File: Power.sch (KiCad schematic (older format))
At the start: 11 parts, among them P1 24-pin Mini-Fit Jr., SW1 SWITCH_INV

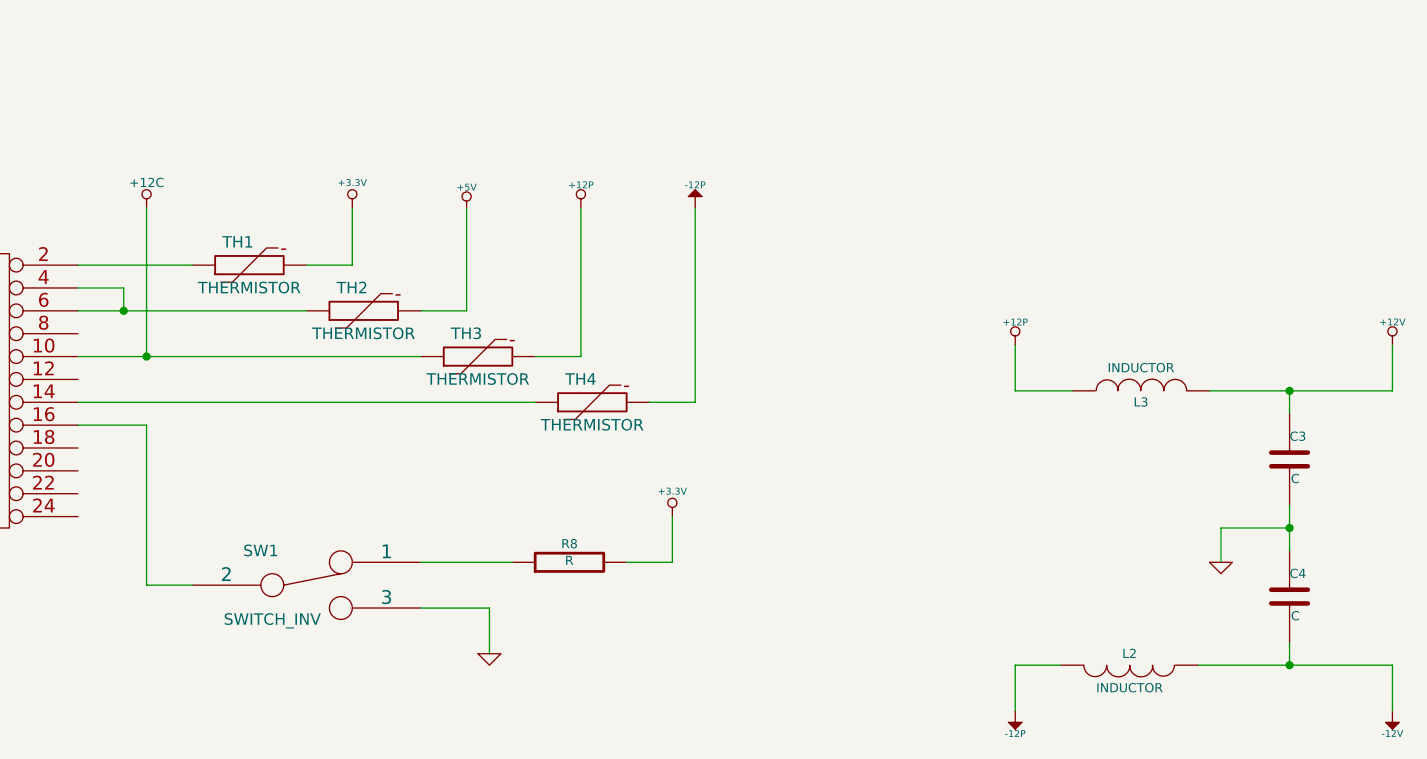
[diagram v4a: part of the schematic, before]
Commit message: Associated and placed the Power Filter Module
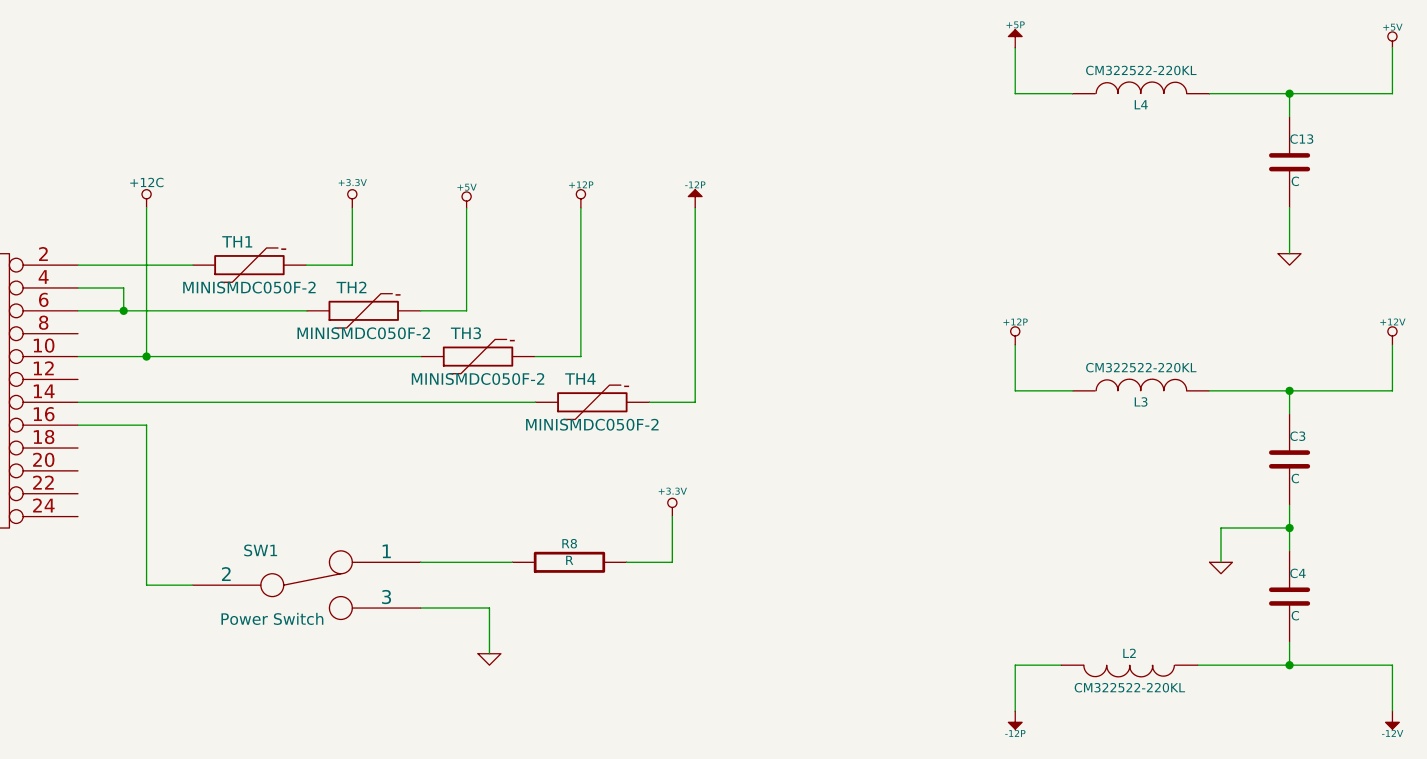
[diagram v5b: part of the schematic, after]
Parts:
- added C13: C, symbol C
- added L4: CM322522-220KL, symbol INDUCTOR
- L2, L3: value INDUCTOR -> CM322522-220KL; MFG Name (none) -> Bourns
- SW1: value SWITCH_INV -> Power Switch; MFG Name (none) -> C&K Components; MFG Part Number (none) -> OS102011MA1QN1
- TH1, TH2, TH3, TH4: value THERMISTOR -> MINISMDC050F-2; MFG Name (none) -> TE Connectivity; MFG Part Number (none) -> MINISMDC050F-2
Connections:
- net +5V: now also C13.1, L4.2
- net GND: now also C13.2
- new net +5P: L4.1
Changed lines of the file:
@@
 P 3500 3200
 F 0 "SW1" H 3300 3350 50  0000 C CNN
-F 1 "SWITCH_INV" H 3350 3050 50  0000 C CNN
+F 1 "Power Switch" H 3350 3050 50  0000 C CNN
 F 2 "" H 3500 3200 60  0000 C CNN
 F 3 "" H 3500 3200 60  0000 C CNN
+F 4 "C&K Components" H 3500 3200 60  0001 C CNN "MFG Name"
+F 5 "OS102011MA1QN1" H 3500 3200 60  0001 C CNN "MFG Part Number"
 	1    3500 3200
 	1    0    0    -1
@@
 $EndComp
 $Comp
-L +12P #PWR15
+L +12P #PWR16
 U 1 1 52F29CEF
 P 6600 2150
-F 0 "#PWR15" H 6600 2120 30  0001 C CNN
+F 0 "#PWR16" H 6600 2120 30  0001 C CNN
 F 1 "+12P" H 6600 2250 30  0000 C CNN
 F 2 "" H 6600 2150 60  0000 C CNN
@@
 $EndComp
 $Comp
-L -12P #PWR16
+L -12P #PWR17
 U 1 1 52F29CF5
 P 6600 3750
-F 0 "#PWR16" H 6600 3880 20  0001 C CNN
+F 0 "#PWR17" H 6600 3880 20  0001 C CNN
 F 1 "-12P" H 6600 3850 30  0000 C CNN
 F 2 "" H 6600 3750 60  0000 C CNN
@@
 $EndComp
 $Comp
-L GND #PWR17
+L GND #PWR18
 U 1 1 52F29CFB
 P 7500 3100
-F 0 "#PWR17" H 7500 3100 30  0001 C CNN
+F 0 "#PWR18" H 7500 3100 30  0001 C CNN
 F 1 "GND" H 7500 3030 30  0001 C CNN
 F 2 "" H 7500 3100 60  0000 C CNN
@@
 P 7150 2350
 F 0 "L3" V 7100 2350 40  0000 C CNN
-F 1 "INDUCTOR" V 7250 2350 40  0000 C CNN
+F 1 "CM322522-220KL" V 7250 2350 40  0000 C CNN
 F 2 "" H 7150 2350 60  0000 C CNN
 F 3 "" H 7150 2350 60  0000 C CNN
+F 4 "Bourns" H 7150 2350 60  0001 C CNN "MFG Name"
 	1    7150 2350
 	0    -1   -1   0
-$EndComp
-$Comp
-L INDUCTOR L2
-U 1 1 52F29D07
-P 7100 3550
-F 0 "L2" V 7050 3550 40  0000 C CNN
-F 1 "INDUCTOR" V 7200 3550 40  0000 C CNN
-F 2 "" H 7100 3550 60  0000 C CNN
-F 3 "" H 7100 3550 60  0000 C CNN
-	1    7100 3550
-	0    1    1    0
 $EndComp
 $Comp
@@
 Connection ~ 7800 3550
 $Comp
-L +12V #PWR18
+L +12V #PWR21
 U 1 1 52F29D29
 P 8250 2150
-F 0 "#PWR18" H 8250 2100 20  0001 C CNN
+F 0 "#PWR21" H 8250 2100 20  0001 C CNN
 F 1 "+12V" H 8250 2250 30  0000 C CNN
 F 2 "" H 8250 2150 60  0000 C CNN
@@
 $EndComp
 $Comp
-L -12V #PWR19
+L -12V #PWR22
 U 1 1 52F29D2F
 P 8250 3750
-F 0 "#PWR19" H 8250 3880 20  0001 C CNN
+F 0 "#PWR22" H 8250 3880 20  0001 C CNN
 F 1 "-12V" H 8250 3850 30  0000 C CNN
 F 2 "" H 8250 3750 60  0000 C CNN
@@
 P 3250 1800
 F 0 "TH1" V 3350 1850 50  0000 C CNN
-F 1 "THERMISTOR" V 3150 1800 50  0000 C CNN
+F 1 "MINISMDC050F-2" V 3150 1800 50  0000 C CNN
 F 2 "" H 3250 1800 60  0000 C CNN
 F 3 "" H 3250 1800 60  0000 C CNN
+F 4 "TE Connectivity" H 3250 1800 60  0001 C CNN "MFG Name"
+F 5 "MINISMDC050F-2" H 3250 1800 60  0001 C CNN "MFG Part Number"
 	1    3250 1800
 	0    -1   -1   0
@@
 $Comp
 L THERMISTOR TH2
-U 1 1 52FBEC68
+U 1 1 530A209B
 P 3750 2000
 F 0 "TH2" V 3850 2050 50  0000 C CNN
-F 1 "THERMISTOR" V 3650 2000 50  0000 C CNN
+F 1 "MINISMDC050F-2" V 3650 2000 50  0000 C CNN
 F 2 "" H 3750 2000 60  0000 C CNN
 F 3 "" H 3750 2000 60  0000 C CNN
+F 4 "TE Connectivity" H 3750 2000 60  0001 C CNN "MFG Name"
+F 5 "MINISMDC050F-2" H 3750 2000 60  0001 C CNN "MFG Part Number"
 	1    3750 2000
 	0    -1   -1   0
@@
 $Comp
 L THERMISTOR TH3
-U 1 1 52FBEC73
+U 1 1 530A20B9
 P 4250 2200
 F 0 "TH3" V 4350 2250 50  0000 C CNN
-F 1 "THERMISTOR" V 4150 2200 50  0000 C CNN
+F 1 "MINISMDC050F-2" V 4150 2200 50  0000 C CNN
 F 2 "" H 4250 2200 60  0000 C CNN
 F 3 "" H 4250 2200 60  0000 C CNN
+F 4 "TE Connectivity" H 4250 2200 60  0001 C CNN "MFG Name"
+F 5 "MINISMDC050F-2" H 4250 2200 60  0001 C CNN "MFG Part Number"
 	1    4250 2200
 	0    -1   -1   0
@@
 $Comp
 L THERMISTOR TH4
-U 1 1 52FBEC7E
+U 1 1 530A20C8
 P 4750 2400
 F 0 "TH4" V 4850 2450 50  0000 C CNN
-F 1 "THERMISTOR" V 4650 2400 50  0000 C CNN
+F 1 "MINISMDC050F-2" V 4650 2400 50  0000 C CNN
 F 2 "" H 4750 2400 60  0000 C CNN
 F 3 "" H 4750 2400 60  0000 C CNN
+F 4 "TE Connectivity" H 4750 2400 60  0001 C CNN "MFG Name"
+F 5 "MINISMDC050F-2" H 4750 2400 60  0001 C CNN "MFG Part Number"
 	1    4750 2400
 	0    -1   -1   0
 $EndComp
+$Comp
+L INDUCTOR L4
+U 1 1 530A2152
+P 7150 1050
+F 0 "L4" V 7100 1050 40  0000 C CNN
+F 1 "CM322522-220KL" V 7250 1050 40  0000 C CNN
+F 2 "" H 7150 1050 60  0000 C CNN
+F 3 "" H 7150 1050 60  0000 C CNN
+F 4 "Bourns" H 7150 1050 60  0001 C CNN "MFG Name"
+	1    7150 1050
+	0    -1   -1   0
+$EndComp
+$Comp
+L C C13
+U 1 1 530A2158
+P 7800 1350
+F 0 "C13" H 7800 1450 40  0000 L CNN
+F 1 "C" H 7806 1265 40  0000 L CNN
+F 2 "" H 7838 1200 30  0000 C CNN
+F 3 "" H 7800 1350 60  0000 C CNN
+	1    7800 1350
+	1    0    0    -1
+$EndComp
+Wire Wire Line
+	7450 1050 8250 1050
+Wire Wire Line
+	7800 1050 7800 1150
+Wire Wire Line
+	7800 1550 7800 1750
+Wire Wire Line
+	6850 1050 6600 1050
+Wire Wire Line
+	6600 1050 6600 850
+Wire Wire Line
+	8250 1050 8250 850
+Connection ~ 7800 1050
+$Comp
+L +5P #PWR15
+U 1 1 530A216D
+P 6600 850
+F 0 "#PWR15" H 6600 980 20  0001 C CNN
+F 1 "+5P" H 6600 950 30  0000 C CNN
+F 2 "" H 6600 850 60  0000 C CNN
+F 3 "" H 6600 850 60  0000 C CNN
+	1    6600 850
+	1    0    0    -1
+$EndComp
+$Comp
+L +5V #PWR20
+U 1 1 530A2195
+P 8250 850
+F 0 "#PWR20" H 8250 940 20  0001 C CNN
+F 1 "+5V" H 8250 940 30  0000 C CNN
+F 2 "" H 8250 850 60  0000 C CNN
+F 3 "" H 8250 850 60  0000 C CNN
+	1    8250 850
+	1    0    0    -1
+$EndComp
+$Comp
+L GND #PWR19
+U 1 1 530A21B1
+P 7800 1750
+F 0 "#PWR19" H 7800 1750 30  0001 C CNN
+F 1 "GND" H 7800 1680 30  0001 C CNN
+F 2 "" H 7800 1750 60  0000 C CNN
+F 3 "" H 7800 1750 60  0000 C CNN
+	1    7800 1750
+	1    0    0    -1
+$EndComp
+$Comp
+L INDUCTOR L2
+U 1 1 530A21BD
+P 7100 3550
+F 0 "L2" V 7050 3550 40  0000 C CNN
+F 1 "CM322522-220KL" V 7200 3550 40  0000 C CNN
+F 2 "" H 7100 3550 60  0000 C CNN
+F 3 "" H 7100 3550 60  0000 C CNN
+F 4 "Bourns" H 7100 3550 60  0001 C CNN "MFG Name"
+	1    7100 3550
+	0    1    1    0
+$EndComp
 $EndSCHEMATC

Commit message: Updates from Layout Work Session 5 video
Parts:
- added TP1: CONN_1, symbol CONN_1
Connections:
- net GND: now also TP1.1
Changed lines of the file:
@@
 $EndComp
 Wire Wire Line
-	1700 1900 900  1900
+	900  1900 1700 1900
 Wire Wire Line
 	1700 2000 1500 2000
@@
 	0    1    1    0
 $EndComp
+$Comp
+L CONN_1 TP1
+U 1 1 53163E2C
+P 5500 4150
+F 0 "TP1" H 5580 4150 40  0000 L CNN
+F 1 "CONN_1" H 5500 4205 30  0001 C CNN
+F 2 "" H 5500 4150 60  0000 C CNN
+F 3 "" H 5500 4150 60  0000 C CNN
+	1    5500 4150
+	-1   0    0    1
+$EndComp
+$Comp
+L GND #PWR021
+U 1 1 53163E4D
+P 5750 4350
+F 0 "#PWR021" H 5750 4350 30  0001 C CNN
+F 1 "GND" H 5750 4280 30  0001 C CNN
+F 2 "" H 5750 4350 60  0000 C CNN
+F 3 "" H 5750 4350 60  0000 C CNN
+	1    5750 4350
+	1    0    0    -1
+$EndComp
+Wire Wire Line
+	5650 4150 5750 4150
+Wire Wire Line
+	5750 4150 5750 4350
 $EndSCHEMATC

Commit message: Updates from Layout Work Session 6 video
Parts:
- added JP1, JP2, JP3, JP4: JUMPER, symbol JUMPER
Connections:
- net +5P: now also TH2.2
- net +5V: no longer TH2.2
- net GND: now also JP1.1, JP2.1, JP3.1, JP4.1
- net at P1.12 (P12): now also P1.2 (P2), TH1.1
- new net AGND: JP1.2
- new net GND_LED: JP3.2
- new net GND_PWR: JP2.2
- new net GND_RELAY: JP4.2
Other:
- note added: "Star Point"
- moved on the sheet: TP1
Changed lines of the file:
@@
-	1    0    0    -1
-$EndComp
-$Comp
-L +3.3V #PWR07
-U 1 1 52F29C8B
-P 3700 1550
-F 0 "#PWR07" H 3700 1510 30  0001 C CNN
-F 1 "+3.3V" H 3700 1660 30  0000 C CNN
-F 2 "" H 3700 1550 60  0000 C CNN
-F 3 "" H 3700 1550 60  0000 C CNN
-	1    3700 1550
-	1    0    0    -1
-$EndComp
-$Comp
-L +5V #PWR08
-U 1 1 52F29C91
-P 4200 1550
-F 0 "#PWR08" H 4200 1640 20  0001 C CNN
-F 1 "+5V" H 4200 1640 30  0000 C CNN
-F 2 "" H 4200 1550 60  0000 C CNN
-F 3 "" H 4200 1550 60  0000 C CNN
-	1    4200 1550
 	1    0    0    -1
 $EndComp
@@
 	4700 2200 4700 1550
 $Comp
-L +12P #PWR09
+L +12P #PWR07
 U 1 1 52F29CC3
 P 4700 1550
-F 0 "#PWR09" H 4700 1520 30  0001 C CNN
+F 0 "#PWR07" H 4700 1520 30  0001 C CNN
 F 1 "+12P" H 4700 1650 30  0000 C CNN
 F 2 "" H 4700 1550 60  0000 C CNN
@@
 	5200 2400 5200 1550
 $Comp
-L -12P #PWR010
+L -12P #PWR08
 U 1 1 52F29CCB
 P 5200 1550
-F 0 "#PWR010" H 5200 1680 20  0001 C CNN
+F 0 "#PWR08" H 5200 1680 20  0001 C CNN
 F 1 "-12P" H 5200 1650 30  0000 C CNN
 F 2 "" H 5200 1550 60  0000 C CNN
@@
 	4300 3300 4300 3500
 $Comp
-L GND #PWR011
+L GND #PWR09
 U 1 1 52F29CDA
 P 4300 3500
-F 0 "#PWR011" H 4300 3500 30  0001 C CNN
+F 0 "#PWR09" H 4300 3500 30  0001 C CNN
 F 1 "GND" H 4300 3430 30  0001 C CNN
 F 2 "" H 4300 3500 60  0000 C CNN
@@
 	5100 3100 5100 2900
 $Comp
-L +3.3V #PWR012
+L +3.3V #PWR010
 U 1 1 52F29CE9
 P 5100 2900
-F 0 "#PWR012" H 5100 2860 30  0001 C CNN
+F 0 "#PWR010" H 5100 2860 30  0001 C CNN
 F 1 "+3.3V" H 5100 3010 30  0000 C CNN
 F 2 "" H 5100 2900 60  0000 C CNN
@@
 $EndComp
 $Comp
-L +12P #PWR013
+L +12P #PWR011
 U 1 1 52F29CEF
 P 6600 2150
-F 0 "#PWR013" H 6600 2120 30  0001 C CNN
+F 0 "#PWR011" H 6600 2120 30  0001 C CNN
 F 1 "+12P" H 6600 2250 30  0000 C CNN
 F 2 "" H 6600 2150 60  0000 C CNN
@@
 $EndComp
 $Comp
-L -12P #PWR014
+L -12P #PWR012
 U 1 1 52F29CF5
 P 6600 3750
-F 0 "#PWR014" H 6600 3880 20  0001 C CNN
+F 0 "#PWR012" H 6600 3880 20  0001 C CNN
 F 1 "-12P" H 6600 3850 30  0000 C CNN
 F 2 "" H 6600 3750 60  0000 C CNN
@@
 $EndComp
 $Comp
-L GND #PWR015
+L GND #PWR013
 U 1 1 52F29CFB
 P 7500 3100
-F 0 "#PWR015" H 7500 3100 30  0001 C CNN
+F 0 "#PWR013" H 7500 3100 30  0001 C CNN
 F 1 "GND" H 7500 3030 30  0001 C CNN
 F 2 "" H 7500 3100 60  0000 C CNN
@@
 Connection ~ 7800 3550
 $Comp
-L +12V #PWR016
+L +12V #PWR014
 U 1 1 52F29D29
 P 8250 2150
-F 0 "#PWR016" H 8250 2100 20  0001 C CNN
+F 0 "#PWR014" H 8250 2100 20  0001 C CNN
 F 1 "+12V" H 8250 2250 30  0000 C CNN
 F 2 "" H 8250 2150 60  0000 C CNN
@@
 $EndComp
 $Comp
-L -12V #PWR017
+L -12V #PWR015
 U 1 1 52F29D2F
 P 8250 3750
-F 0 "#PWR017" H 8250 3880 20  0001 C CNN
+F 0 "#PWR015" H 8250 3880 20  0001 C CNN
 F 1 "-12V" H 8250 3850 30  0000 C CNN
 F 2 "" H 8250 3750 60  0000 C CNN
@@
 	2800 2200 2800 1550
 $Comp
-L +12C #PWR018
+L +12C #PWR016
 U 1 1 52FBE7EF
 P 2800 1550
-F 0 "#PWR018" H 2800 1520 30  0001 C CNN
+F 0 "#PWR016" H 2800 1520 30  0001 C CNN
 F 1 "+12C" H 2800 1660 40  0000 C CNN
 F 2 "" H 2800 1550 60  0000 C CNN
@@
 Connection ~ 7800 1050
 $Comp
-L +5P #PWR15
+L +5P #PWR20
 U 1 1 530A216D
 P 6600 850
-F 0 "#PWR15" H 6600 980 20  0001 C CNN
+F 0 "#PWR20" H 6600 980 20  0001 C CNN
 F 1 "+5P" H 6600 950 30  0000 C CNN
 F 2 "" H 6600 850 60  0000 C CNN
@@
 $EndComp
 $Comp
-L +5V #PWR019
+L +5V #PWR017
 U 1 1 530A2195
 P 8250 850
-F 0 "#PWR019" H 8250 940 20  0001 C CNN
+F 0 "#PWR017" H 8250 940 20  0001 C CNN
 F 1 "+5V" H 8250 940 30  0000 C CNN
 F 2 "" H 8250 850 60  0000 C CNN
@@
 $EndComp
 $Comp
-L GND #PWR020
+L GND #PWR018
 U 1 1 530A21B1
 P 7800 1750
-F 0 "#PWR020" H 7800 1750 30  0001 C CNN
+F 0 "#PWR018" H 7800 1750 30  0001 C CNN
 F 1 "GND" H 7800 1680 30  0001 C CNN
 F 2 "" H 7800 1750 60  0000 C CNN
@@
 L CONN_1 TP1
 U 1 1 53163E2C
-P 5500 4150
-F 0 "TP1" H 5580 4150 40  0000 L CNN
-F 1 "CONN_1" H 5500 4205 30  0001 C CNN
-F 2 "" H 5500 4150 60  0000 C CNN
-F 3 "" H 5500 4150 60  0000 C CNN
-	1    5500 4150
-	-1   0    0    1
-$EndComp
-$Comp
-L GND #PWR021
-U 1 1 53163E4D
-P 5750 4350
-F 0 "#PWR021" H 5750 4350 30  0001 C CNN
-F 1 "GND" H 5750 4280 30  0001 C CNN
-F 2 "" H 5750 4350 60  0000 C CNN
-F 3 "" H 5750 4350 60  0000 C CNN
-	1    5750 4350
-	1    0    0    -1
-$EndComp
-Wire Wire Line
-	5650 4150 5750 4150
-Wire Wire Line
-	5750 4150 5750 4350
+P 3000 5150
+F 0 "TP1" H 3080 5150 40  0000 L CNN
+F 1 "CONN_1" H 3000 5205 30  0001 C CNN
+F 2 "" H 3000 5150 60  0000 C CNN
+F 3 "" H 3000 5150 60  0000 C CNN
+	1    3000 5150
+	0    -1   -1   0
+$EndComp
+Wire Wire Line
+	2500 2300 2600 2300
+Wire Wire Line
+	2600 2300 2600 1800
+Connection ~ 2600 1800
+$Comp
+L +5P #PWR11
+U 1 1 53164D37
+P 4200 1550
+F 0 "#PWR11" H 4200 1680 20  0001 C CNN
+F 1 "+5P" H 4200 1650 30  0000 C CNN
+F 2 "" H 4200 1550 60  0000 C CNN
+F 3 "" H 4200 1550 60  0000 C CNN
+	1    4200 1550
+	1    0    0    -1
+$EndComp
+$Comp
+L +3.3V #PWR019
+U 1 1 52F29C8B
+P 3700 1550
+F 0 "#PWR019" H 3700 1510 30  0001 C CNN
+F 1 "+3.3V" H 3700 1660 30  0000 C CNN
+F 2 "" H 3700 1550 60  0000 C CNN
+F 3 "" H 3700 1550 60  0000 C CNN
+	1    3700 1550
+	1    0    0    -1
+$EndComp
+Text Notes 3700 4700 0    60   ~ 0
+Star Point
+$Comp
+L JUMPER JP1
+U 1 1 531653CA
+P 3700 5700
+F 0 "JP1" H 3700 5850 60  0000 C CNN
+F 1 "JUMPER" H 3700 5620 40  0000 C CNN
+F 2 "" H 3700 5700 60  0000 C CNN
+F 3 "" H 3700 5700 60  0000 C CNN
+	1    3700 5700
+	1    0    0    -1
+$EndComp
+$Comp
+L JUMPER JP2
+U 1 1 531653DC
+P 3700 6100
+F 0 "JP2" H 3700 6250 60  0000 C CNN
+F 1 "JUMPER" H 3700 6020 40  0000 C CNN
+F 2 "" H 3700 6100 60  0000 C CNN
+F 3 "" H 3700 6100 60  0000 C CNN
+	1    3700 6100
+	1    0    0    -1
+$EndComp
+$Comp
+L JUMPER JP3
+U 1 1 531653E7
+P 3700 6500
+F 0 "JP3" H 3700 6650 60  0000 C CNN
+F 1 "JUMPER" H 3700 6420 40  0000 C CNN
+F 2 "" H 3700 6500 60  0000 C CNN
+F 3 "" H 3700 6500 60  0000 C CNN
+	1    3700 6500
+	1    0    0    -1
+$EndComp
+$Comp
+L JUMPER JP4
+U 1 1 531653F2
+P 3700 6900
+F 0 "JP4" H 3700 7050 60  0000 C CNN
+F 1 "JUMPER" H 3700 6820 40  0000 C CNN
+F 2 "" H 3700 6900 60  0000 C CNN
+F 3 "" H 3700 6900 60  0000 C CNN
+	1    3700 6900
+	1    0    0    -1
+$EndComp
+Wire Wire Line
+	3400 5700 3000 5700
+Wire Wire Line
+	3000 5300 3000 7200
+$Comp
+L GND #PWR020
+U 1 1 5316543C
+P 3000 7200
+F 0 "#PWR020" H 3000 7200 30  0001 C CNN
+F 1 "GND" H 3000 7130 30  0001 C CNN
+F 2 "" H 3000 7200 60  0000 C CNN
+F 3 "" H 3000 7200 60  0000 C CNN
+	1    3000 7200
+	1    0    0    -1
+$EndComp
+Wire Wire Line
+	3400 6100 3000 6100
+Connection ~ 3000 6100
+Wire Wire Line
+	3400 6500 3000 6500
+Connection ~ 3000 6500
+Wire Wire Line
+	3400 6900 3000 6900
+Connection ~ 3000 6900
+Wire Wire Line
+	4000 5700 4400 5700
+Wire Wire Line
+	4400 5700 4400 5900
+Wire Wire Line
+	4000 6100 4400 6100
+Wire Wire Line
+	4400 6100 4400 6300
+Wire Wire Line
+	4000 6500 4400 6500
+Wire Wire Line
+	4400 6500 4400 6700
+Wire Wire Line
+	4000 6900 4400 6900
+Wire Wire Line
+	4400 6900 4400 7100
+$Comp
+L AGND #PWR021
+U 1 1 5316559F
+P 4400 5900
+F 0 "#PWR021" H 4400 5900 40  0001 C CNN
+F 1 "AGND" H 4400 5830 50  0000 C CNN
+F 2 "" H 4400 5900 60  0000 C CNN
+F 3 "" H 4400 5900 60  0000 C CNN
+	1    4400 5900
+	1    0    0    -1
+$EndComp
+$Comp
+L GND_PWR #PWR022
+U 1 1 531655B3
+P 4400 6300
+F 0 "#PWR022" H 4400 6300 30  0001 C CNN
+F 1 "GND_PWR" H 4400 6230 30  0000 C CNN
+F 2 "" H 4400 6300 60  0000 C CNN
+F 3 "" H 4400 6300 60  0000 C CNN
+	1    4400 6300
+	1    0    0    -1
+$EndComp
+$Comp
+L GND_LED #PWR023
+U 1 1 531655C7
+P 4400 6700
+F 0 "#PWR023" H 4400 6700 30  0001 C CNN
+F 1 "GND_LED" H 4400 6630 30  0000 C CNN
+F 2 "" H 4400 6700 60  0000 C CNN
+F 3 "" H 4400 6700 60  0000 C CNN
+	1    4400 6700
+	1    0    0    -1
+$EndComp
+$Comp
+L GND_RELAY #PWR024
+U 1 1 531655DB
+P 4400 7100
+F 0 "#PWR024" H 4400 7100 30  0001 C CNN
+F 1 "GND_RELAY" H 4400 7030 30  0000 C CNN
+F 2 "" H 4400 7100 60  0000 C CNN
+F 3 "" H 4400 7100 60  0000 C CNN
+	1    4400 7100
+	1    0    0    -1
+$EndComp
+Connection ~ 3000 5700
 $EndSCHEMATC
